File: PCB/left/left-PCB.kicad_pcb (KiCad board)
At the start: 2 copper layers, 137.8 x 95 mm, 50 parts, among them J1 Modulo-Jack, J2 Modulo-Jack, SW1 SW_Push, SW10 SW_Push, SW11 SW_Push, SW12 SW_Push, SW13 SW_Push, SW14 SW_Push, SW15 SW_Push, SW16 SW_Push, SW17 SW_Push, SW18 SW_Push, SW19 SW_Push, SW2 SW_Push, SW20 SW_Push, SW21 SW_Push, SW22 SW_Push, SW23 SW_Push, SW24 SW_Push, SW25 SW_Push, SW26 SW_Push, SW27 SW_Push, SW28 SW_Push, SW3 SW_Push, SW30 SW_Push, SW31 SW_Push, SW32 SW_Push, SW4 SW_Push, SW5 SW_Push, SW50 SW_DIP_x04, SW6 SW_Push, SW7 SW_Push, SW8 SW_Push, SW9 SW_Push, U1 MCP23017_SP, U2 MCP23017_SP

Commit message: add sign
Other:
- board text added: "satsuma JP SMD rev.1 Designed by @ysni_pub"
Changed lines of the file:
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@@
   (general
     (thickness 1.6)
-    (drawings 23)
+    (drawings 24)
     (tracks 572)
     (zones 0)
@@
     (pad "" np_thru_hole circle (at 2.54 -5.08) (size 3 3) (drill 3) (layers *.Cu *.Mask))
   )
+  (gr_text "satsuma JP SMD rev.1    Designed by @ysni_pub" (at 111.76 150.495) (layer F.SilkS)
+    (effects (font (size 1.5 1.5) (thickness 0.15)))
+  )
   (gr_circle (center 99.775 76.025) (end 102.125133 76.025) (layer Dwgs.User) (width 0.15))
   (dimension 95 (width 0.15) (layer Dwgs.User)
@@
   (segment (start 145.675 90.35) (end 145.675 88.005) (width 0.5) (layer B.Cu) (net 1))
   (segment (start 145.675 88.005) (end 146.685 86.995) (width 0.5) (layer B.Cu) (net 1))
-  (via (at 163.83 88.9) (size 0.8) (drill 0.4) (layers F.Cu B.Cu) (net 2))
-  (segment (start 163.445 89.285) (end 163.83 88.9) (width 0.5) (layer B.Cu) (net 2))
-  (segment (start 163.445 91.19) (end 163.445 89.285) (width 0.5) (layer B.Cu) (net 2))
-  (segment (start 163.445 91.19) (end 164.04 91.19) (width 0.5) (layer B.Cu) (net 2))
-  (segment (start 162.77 91.19) (end 163.445 91.19) (width 0.5) (layer B.Cu) (net 2))
   (segment (start 140.97 119.442) (end 135.859 114.331) (width 0.5) (layer F.Cu) (net 1))
   (via (at 135.859 114.331) (size 0.8) (drill 0.4) (layers F.Cu B.Cu) (net 1))
@@
   (segment (start 193.675 102.235) (end 195.2625 100.6475) (width 0.5) (layer B.Cu) (net 1))
   (segment (start 195.2625 100.6475) (end 195.58 100.33) (width 0.5) (layer B.Cu) (net 1))
+  (via (at 163.83 88.9) (size 0.8) (drill 0.4) (layers F.Cu B.Cu) (net 2))
+  (segment (start 163.445 89.285) (end 163.83 88.9) (width 0.5) (layer B.Cu) (net 2))
+  (segment (start 163.445 91.19) (end 163.445 89.285) (width 0.5) (layer B.Cu) (net 2))
+  (segment (start 163.445 91.19) (end 164.04 91.19) (width 0.5) (layer B.Cu) (net 2))
+  (segment (start 162.77 91.19) (end 163.445 91.19) (width 0.5) (layer B.Cu) (net 2))
   (segment (start 144.405 90.35) (end 144.405 91.815) (width 0.5) (layer B.Cu) (net 2))
   (segment (start 144.405 91.815) (end 140.335 95.885) (width 0.5) (layer B.Cu) (net 2))

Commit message: add silk
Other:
- board text added: "1"
- board text added: "1MΩ"
- board text added: "1μF"
- board text added: "2"
- board text added: "A"
- board text added: "ADDR"
- board text added: "CapsLock"
- board text added: "KHS42E"
- board text added: "LED"
- board text added: "MCP23017-E/SO"
- board text added: "OFF"
- board text added: "ON"
- board text added: "POWER"
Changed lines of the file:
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@@
   (general
     (thickness 1.6)
-    (drawings 24)
+    (drawings 43)
     (tracks 572)
     (zones 0)
@@
     (descr "Resistor, Axial_DIN0207 series, Axial, Horizontal, pin pitch=10.16mm, 0.25W = 1/4W, length*diameter=6.3*2.5mm^2, http://cdn-reichelt.de/documents/datenblatt/B400/1_4W%23YAG.pdf")
     (tags "Resistor Axial_DIN0207 series Axial Horizontal pin pitch 10.16mm 0.25W = 1/4W length 6.3mm diameter 2.5mm")
-    (fp_text reference R3 (at 5.08 -2.37) (layer F.SilkS)
+    (fp_text reference R3 (at 5.08 2.375) (layer F.SilkS)
       (effects (font (size 1 1) (thickness 0.15)))
     )
@@
     (descr "Resistor, Axial_DIN0207 series, Axial, Horizontal, pin pitch=10.16mm, 0.25W = 1/4W, length*diameter=6.3*2.5mm^2, http://cdn-reichelt.de/documents/datenblatt/B400/1_4W%23YAG.pdf")
     (tags "Resistor Axial_DIN0207 series Axial Horizontal pin pitch 10.16mm 0.25W = 1/4W length 6.3mm diameter 2.5mm")
-    (fp_text reference R1 (at 5.08 -2.37) (layer F.SilkS)
+    (fp_text reference R1 (at 5.08 2.375) (layer F.SilkS)
       (effects (font (size 1 1) (thickness 0.15)))
     )
@@
     (pad "" np_thru_hole circle (at 2.54 -5.08) (size 3 3) (drill 3) (layers *.Cu *.Mask))
   )
+  (gr_text A (at 165.735 89.535) (layer B.SilkS)
+    (effects (font (size 1 1) (thickness 0.15)) (justify mirror))
+  )
+  (gr_text KHS42E (at 161.925 94.615) (layer B.SilkS)
+    (effects (font (size 1 1) (thickness 0.15)) (justify mirror))
+  )
+  (gr_text OFF (at 166.37 99.06) (layer B.SilkS)
+    (effects (font (size 1 1) (thickness 0.15)) (justify mirror))
+  )
+  (gr_text ON (at 166.37 91.44) (layer B.SilkS)
+    (effects (font (size 1 1) (thickness 0.15)) (justify mirror))
+  )
+  (gr_text 2 (at 164.465 89.535) (layer B.SilkS)
+    (effects (font (size 1 1) (thickness 0.15)) (justify mirror))
+  )
+  (gr_text 1 (at 162.56 89.535) (layer B.SilkS)
+    (effects (font (size 1 1) (thickness 0.15)) (justify mirror))
+  )
+  (gr_text 1MΩ (at 193.675 95.25) (layer F.SilkS)
+    (effects (font (size 1 1) (thickness 0.15)))
+  )
+  (gr_text 1MΩ (at 176.53 95.25) (layer F.SilkS)
+    (effects (font (size 1 1) (thickness 0.15)))
+  )
+  (gr_text 1μF (at 137.16 74.295) (layer B.SilkS)
+    (effects (font (size 1 1) (thickness 0.15)) (justify mirror))
+  )
+  (gr_text MCP23017-E/SO (at 142.24 133.985) (layer B.SilkS)
+    (effects (font (size 1 1) (thickness 0.2)) (justify mirror))
+  )
+  (gr_text MCP23017-E/SO (at 142.24 93.345) (layer B.SilkS)
+    (effects (font (size 1 1) (thickness 0.2)) (justify mirror))
+  )
+  (gr_text CapsLock (at 83.185 106.045 270) (layer B.SilkS)
+    (effects (font (size 1 1) (thickness 0.15)) (justify mirror))
+  )
+  (gr_text CapsLock (at 83.185 106.045 -90) (layer F.SilkS)
+    (effects (font (size 1 1) (thickness 0.15)))
+  )
+  (gr_text POWER (at 82.55 125.095 270) (layer B.SilkS)
+    (effects (font (size 1 1) (thickness 0.15)) (justify mirror))
+  )
+  (gr_text POWER (at 82.55 125.095 270) (layer F.SilkS)
+    (effects (font (size 1 1) (thickness 0.15)))
+  )
+  (gr_text ADDR (at 193.675 97.375) (layer F.SilkS)
+    (effects (font (size 1 1) (thickness 0.15)))
+  )
+  (gr_text ADDR (at 176.53 97.375) (layer F.SilkS)
+    (effects (font (size 1 1) (thickness 0.15)))
+  )
+  (gr_text LED (at 120.65 97.375) (layer F.SilkS)
+    (effects (font (size 1.5 1.5) (thickness 0.3)))
+  )
+  (gr_text LED (at 104.775 97.79) (layer F.SilkS)
+    (effects (font (size 1.5 1.5) (thickness 0.3)))
+  )
   (gr_text "satsuma JP SMD rev.1    Designed by @ysni_pub" (at 111.76 150.495) (layer F.SilkS)

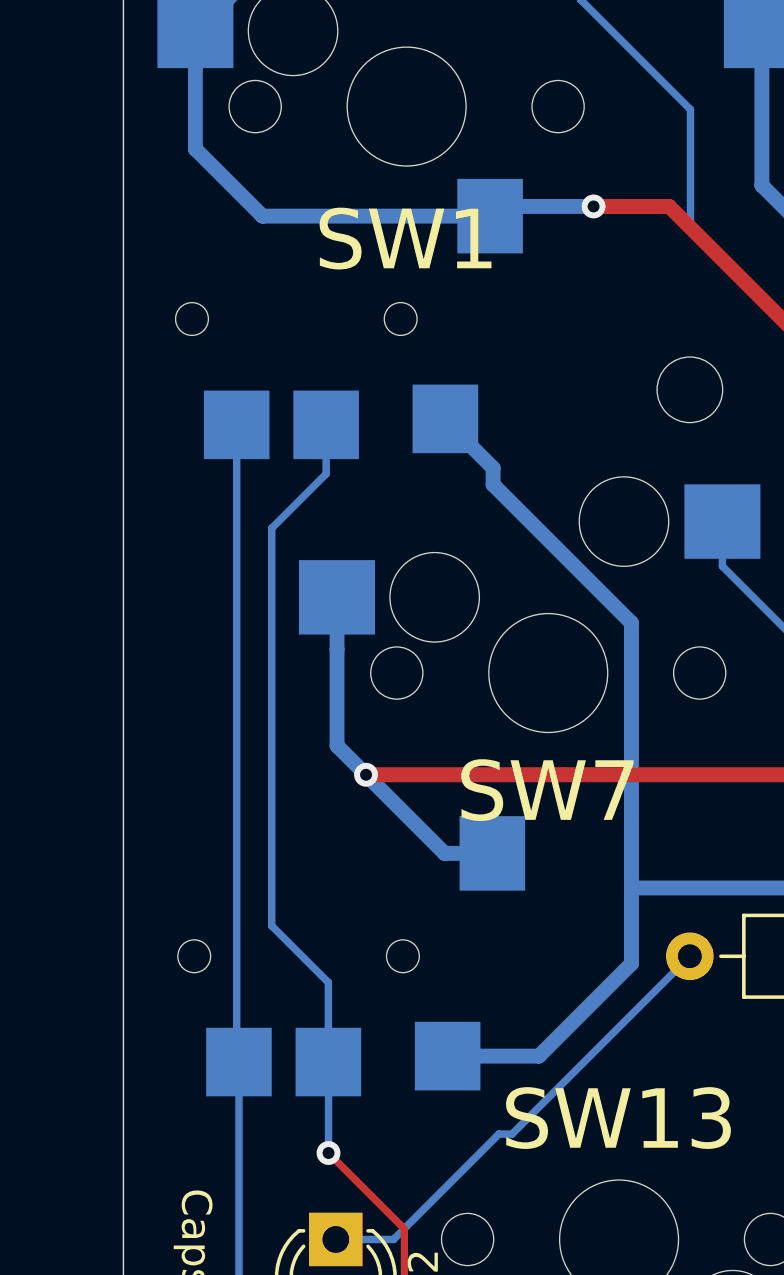
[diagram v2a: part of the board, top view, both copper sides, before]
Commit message: change TRRS jack footprint to PJ-320D
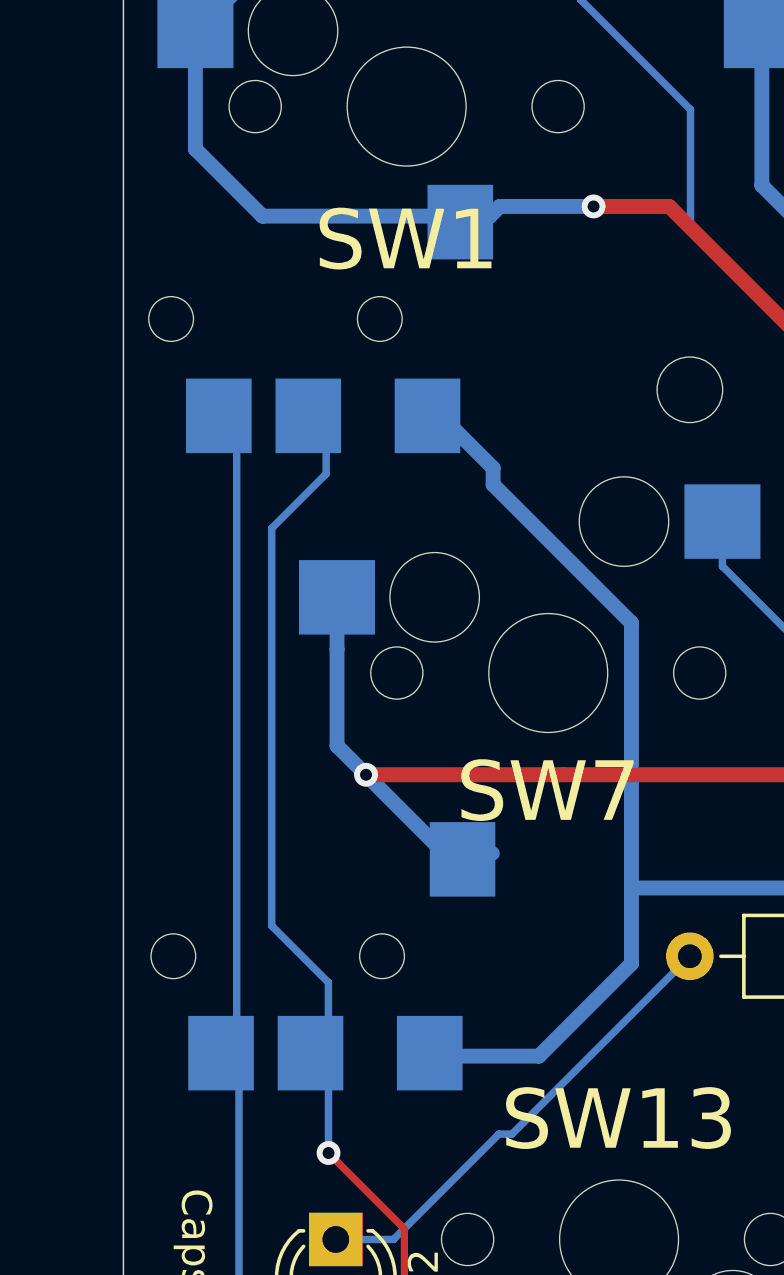
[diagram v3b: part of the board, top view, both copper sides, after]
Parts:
- J1, J2: footprint lib:TRRS_SMD_SJ2-3574A-SMT_ABCD -> lib:PJ-320D
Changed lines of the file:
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@@
     (add_net VCC)
+  )
+  (module lib:PJ-320D (layer B.Cu)
+    (at 80.75 73.625)
+    (fp_text reference J2 (at 6 -6.35) (layer B.SilkS)
+      (effects (font (size 1 1) (thickness 0.15)) (justify mirror))
+    )
+    (fp_text value Modulo-Jack (at 6 6.35) (layer B.Fab)
+      (effects (font (size 1 1) (thickness 0.15)) (justify mirror))
+    )
+    (fp_line (start -2 -2.5) (end 0 -2.5) (layer B.SilkS) (width 0.15))
+    (fp_line (start -2 2.5) (end -2 -2.5) (layer B.SilkS) (width 0.15))
+    (fp_line (start 0 2.5) (end -2 2.5) (layer B.SilkS) (width 0.15))
+    (fp_line (start 0 -3.05) (end 0 3.05) (layer B.SilkS) (width 0.15))
+    (fp_line (start 12.1 -3.05) (end 0 -3.05) (layer B.SilkS) (width 0.15))
+    (fp_line (start 12.1 3.05) (end 12.1 -3.05) (layer B.SilkS) (width 0.15))
+    (fp_line (start 0 3.05) (end 12.1 3.05) (layer B.SilkS) (width 0.15))
+    (pad B smd rect (at 3.2 3.25) (size 2.2 2.5) (layers B.Cu B.Paste B.Mask)
+      (net 3 SDA))
+    (pad C smd rect (at 6.2 3.25) (size 2.2 2.5) (layers B.Cu B.Paste B.Mask)
+      (net 4 SCL))
+    (pad D smd rect (at 10.2 3.25) (size 2.2 2.5) (layers B.Cu B.Paste B.Mask)
+      (net 2 VCC))
+    (pad A smd rect (at 11.3 -3.25) (size 2.2 2.5) (layers B.Cu B.Paste B.Mask)
+      (net 1 GND))
+    (pad "" np_thru_hole circle (at 8.6 0) (size 1.5 1.5) (drill 1.5) (layers *.Cu *.Mask))
+    (pad "" np_thru_hole circle (at 1.6 0) (size 1.5 1.5) (drill 1.5) (layers *.Cu *.Mask))
+  )
+  (module lib:PJ-320D (layer B.Cu)
+    (at 80.825 95)
+    (fp_text reference J1 (at 6 -6.35) (layer B.SilkS)
+      (effects (font (size 1 1) (thickness 0.15)) (justify mirror))
+    )
+    (fp_text value Modulo-Jack (at 6 6.35) (layer B.Fab)
+      (effects (font (size 1 1) (thickness 0.15)) (justify mirror))
+    )
+    (fp_line (start -2 -2.5) (end 0 -2.5) (layer B.SilkS) (width 0.15))
+    (fp_line (start -2 2.5) (end -2 -2.5) (layer B.SilkS) (width 0.15))
+    (fp_line (start 0 2.5) (end -2 2.5) (layer B.SilkS) (width 0.15))
+    (fp_line (start 0 -3.05) (end 0 3.05) (layer B.SilkS) (width 0.15))
+    (fp_line (start 12.1 -3.05) (end 0 -3.05) (layer B.SilkS) (width 0.15))
+    (fp_line (start 12.1 3.05) (end 12.1 -3.05) (layer B.SilkS) (width 0.15))
+    (fp_line (start 0 3.05) (end 12.1 3.05) (layer B.SilkS) (width 0.15))
+    (pad B smd rect (at 3.2 3.25) (size 2.2 2.5) (layers B.Cu B.Paste B.Mask)
+      (net 3 SDA))
+    (pad C smd rect (at 6.2 3.25) (size 2.2 2.5) (layers B.Cu B.Paste B.Mask)
+      (net 4 SCL))
+    (pad D smd rect (at 10.2 3.25) (size 2.2 2.5) (layers B.Cu B.Paste B.Mask)
+      (net 2 VCC))
+    (pad A smd rect (at 11.3 -3.25) (size 2.2 2.5) (layers B.Cu B.Paste B.Mask)
+      (net 1 GND))
+    (pad "" np_thru_hole circle (at 8.6 0) (size 1.5 1.5) (drill 1.5) (layers *.Cu *.Mask))
+    (pad "" np_thru_hole circle (at 1.6 0) (size 1.5 1.5) (drill 1.5) (layers *.Cu *.Mask))
   )
   (module Package_SO:SOIC-28W_7.5x17.9mm_P1.27mm (layer B.Cu)
@@
     )
   )
-  (module lib:TRRS_SMD_SJ2-3574A-SMT_ABCD (layer B.Cu)
-    (at 80.75 73.625)
-    (fp_text reference J2 (at 6 -6.35 180) (layer B.SilkS)
-      (effects (font (size 1 1) (thickness 0.15)) (justify mirror))
-    )
-    (fp_text value Modulo-Jack (at 6 6.35 180) (layer B.Fab)
-      (effects (font (size 1 1) (thickness 0.15)) (justify mirror))
-    )
-    (fp_line (start -1.2 -2.8) (end 0 -2.8) (layer B.SilkS) (width 0.15))
-    (fp_line (start -1.2 2.8) (end -1.2 -2.8) (layer B.SilkS) (width 0.15))
-    (fp_line (start 0 2.8) (end -1.2 2.8) (layer B.SilkS) (width 0.15))
-    (fp_line (start 0 -3) (end 0 3) (layer B.SilkS) (width 0.15))
-    (fp_line (start 13.8 -3) (end 0 -3) (layer B.SilkS) (width 0.15))
-    (fp_line (start 13.8 3) (end 13.8 -3) (layer B.SilkS) (width 0.15))
-    (fp_line (start 0 3) (end 13.8 3) (layer B.SilkS) (width 0.15))
-    (pad B smd rect (at 3.8 3.55) (size 2.2 2.3) (layers B.Cu B.Paste B.Mask)
-      (net 3 SDA))
-    (pad C smd rect (at 6.8 3.55) (size 2.2 2.3) (layers B.Cu B.Paste B.Mask)
-      (net 4 SCL))
-    (pad D smd rect (at 10.8 3.35) (size 2.2 2.3) (layers B.Cu B.Paste B.Mask)
-      (net 2 VCC))
-    (pad A smd rect (at 12.3 -3.45) (size 2.2 2.5) (layers B.Cu B.Paste B.Mask)
-      (net 1 GND))
-    (pad "" np_thru_hole circle (at 9.3 0) (size 1.1 1.1) (drill 1.1) (layers *.Cu *.Mask))
-    (pad "" np_thru_hole circle (at 2.3 0) (size 1.1 1.1) (drill 1.1) (layers *.Cu *.Mask))
-  )
-  (module lib:TRRS_SMD_SJ2-3574A-SMT_ABCD (layer B.Cu)
-    (at 80.825 95)
-    (fp_text reference J1 (at 6 -6.35) (layer B.SilkS)
-      (effects (font (size 1 1) (thickness 0.15)) (justify mirror))
-    )
-    (fp_text value Modulo-Jack (at 6 6.35) (layer B.Fab)
-      (effects (font (size 1 1) (thickness 0.15)) (justify mirror))
-    )
-    (fp_line (start -1.2 -2.8) (end 0 -2.8) (layer B.SilkS) (width 0.15))
-    (fp_line (start -1.2 2.8) (end -1.2 -2.8) (layer B.SilkS) (width 0.15))
-    (fp_line (start 0 2.8) (end -1.2 2.8) (layer B.SilkS) (width 0.15))
-    (fp_line (start 0 -3) (end 0 3) (layer B.SilkS) (width 0.15))
-    (fp_line (start 13.8 -3) (end 0 -3) (layer B.SilkS) (width 0.15))
-    (fp_line (start 13.8 3) (end 13.8 -3) (layer B.SilkS) (width 0.15))
-    (fp_line (start 0 3) (end 13.8 3) (layer B.SilkS) (width 0.15))
-    (pad B smd rect (at 3.8 3.55) (size 2.2 2.3) (layers B.Cu B.Paste B.Mask)
-      (net 3 SDA))
-    (pad C smd rect (at 6.8 3.55) (size 2.2 2.3) (layers B.Cu B.Paste B.Mask)
-      (net 4 SCL))
-    (pad D smd rect (at 10.8 3.35) (size 2.2 2.3) (layers B.Cu B.Paste B.Mask)
-      (net 2 VCC))
-    (pad A smd rect (at 12.3 -3.45) (size 2.2 2.5) (layers B.Cu B.Paste B.Mask)
-      (net 1 GND))
-    (pad "" np_thru_hole circle (at 9.3 0) (size 1.1 1.1) (drill 1.1) (layers *.Cu *.Mask))
-    (pad "" np_thru_hole circle (at 2.3 0) (size 1.1 1.1) (drill 1.1) (layers *.Cu *.Mask))
-  )
   (module Capacitor_SMD:C_2225_5664Metric_Pad1.80x6.60mm_HandSolder (layer B.Cu)

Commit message: move screw holl
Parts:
- moved ? 19.0 mm to (123.5, 133.0)
- moved ? 0.97 mm to (84.5, 133.0)
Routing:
- net Caps: track 71.1 -> 69.5 mm
